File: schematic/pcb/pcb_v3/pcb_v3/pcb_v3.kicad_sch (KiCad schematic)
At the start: 52 parts, among them IC1 FT232RNQ-TRAY, J1 5V, J2 SERVO, J3 MAVLINK, J4 DISPLAY, J5 SER. SERVO, J6 MAG., J7 U.FL-R, J8 Conn_01x05_Pin, J9 Conn_01x05_Pin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

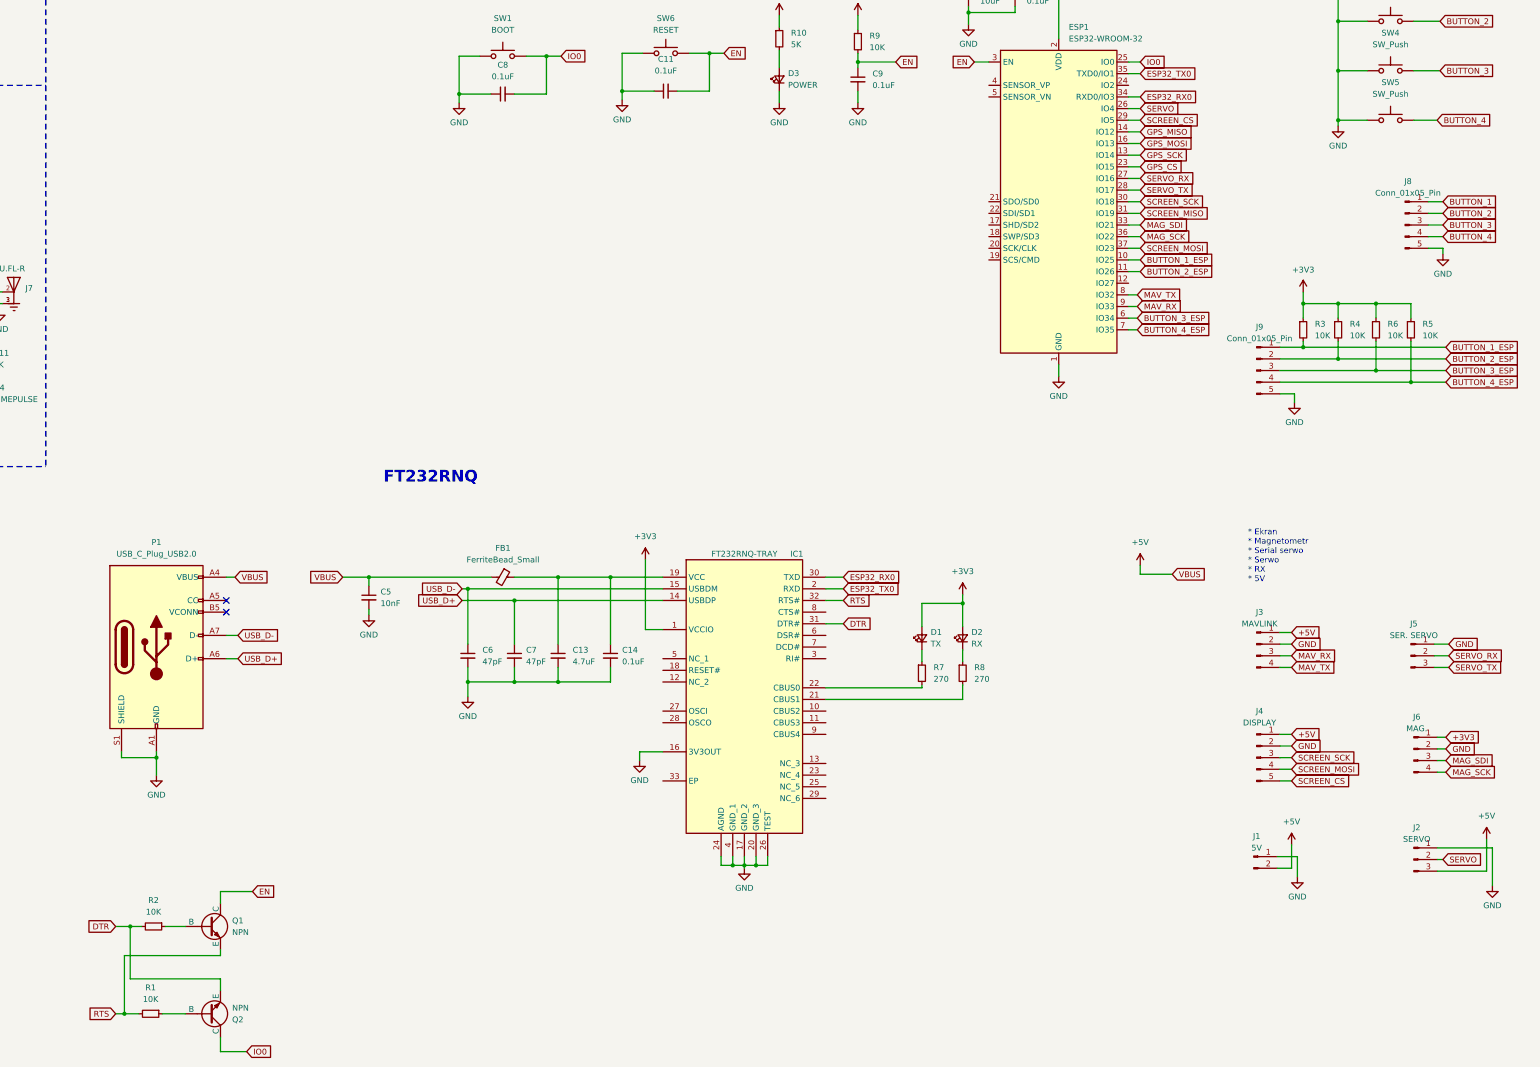
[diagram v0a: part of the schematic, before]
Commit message: pcb update, bluetooth bridge working
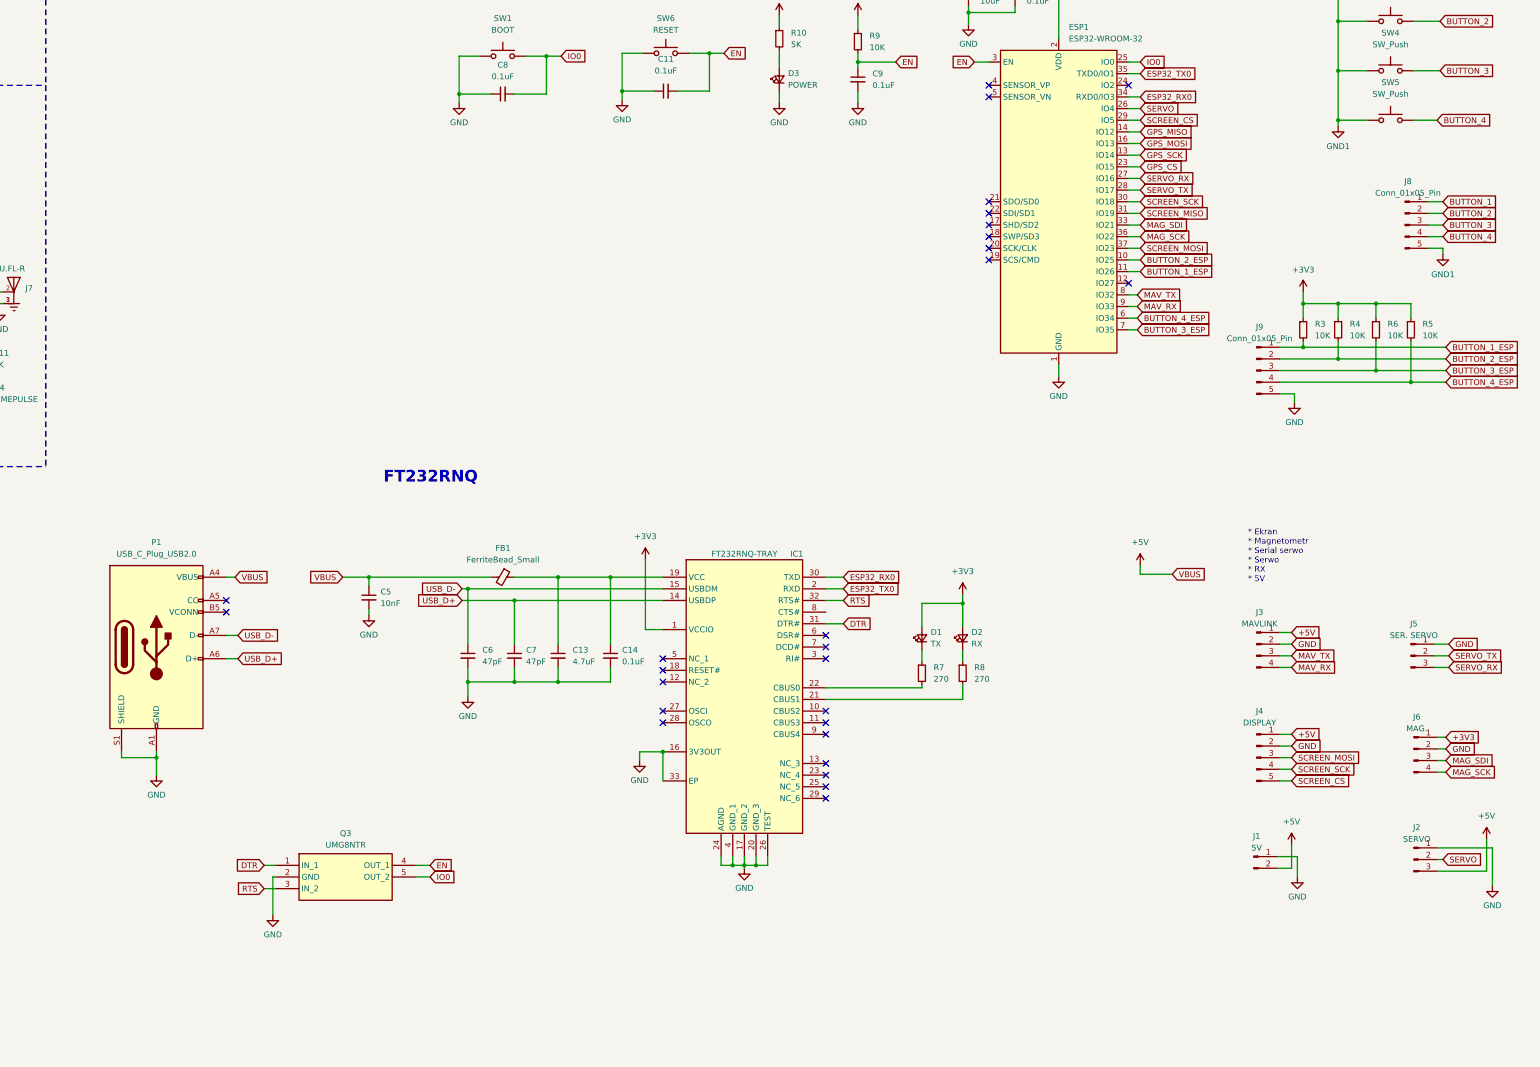
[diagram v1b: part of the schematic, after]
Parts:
- removed Q1, Q2: NPN, Package_TO_SOT_SMD:TSOT-23, symbol Simulation_SPICE:NPN
- removed R1, R2: 10K, Resistor_SMD:R_0805_2012Metric, symbol Device:R_Small
- added Q3: UMG8NTR, Package_TO_SOT_SMD:SOT-353_SC-70-5, symbol Transistor_BJT:UMG8NTR
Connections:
- net BUTTON_1_ESP: now also ESP1.11 (IO26); no longer ESP1.10 (IO25)
- net BUTTON_2_ESP: now also ESP1.10 (IO25); no longer ESP1.11 (IO26)
- net BUTTON_3_ESP: now also ESP1.7 (IO35); no longer ESP1.6 (IO34)
- net BUTTON_4_ESP: now also ESP1.6 (IO34); no longer ESP1.7 (IO35)
- net DTR: now also Q3.1 (IN_1)
- net EN: now also Q3.4 (OUT_1)
- net GND: now also IC1.33 (EP), Q3.2 (GND); no longer J8.5 (Pin_5), SW2.1, SW3.1, SW4.1, SW5.1
- net IO0: now also Q3.5 (OUT_2)
- net MAV_RX: now also J3.4 (Pin_4); no longer J3.3 (Pin_3)
- net MAV_TX: now also J3.3 (Pin_3); no longer J3.4 (Pin_4)
- net RTS: now also Q3.3 (IN_2)
- net SCREEN_MOSI: now also J4.3 (Pin_3); no longer J4.4 (Pin_4)
- net SCREEN_SCK: now also J4.4 (Pin_4); no longer J4.3 (Pin_3)
- net SERVO_RX: now also J5.3 (Pin_3); no longer J5.2 (Pin_2)
- net SERVO_TX: now also J5.2 (Pin_2); no longer J5.3 (Pin_3)
- new net GND1: J8.5 (Pin_5), SW2.1, SW3.1, SW4.1, SW5.1
- no-connect marks 9 -> 34

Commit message: pcb updates
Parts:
- removed Q3: UMG8NTR, Package_TO_SOT_SMD:SOT-353_SC-70-5, symbol Transistor_BJT:UMG8NTR
- added BT1: Battery_Cell, Battery:BatteryHolder_Keystone_1060_1x2032, symbol Device:Battery_Cell
- added C15: 0.1uF, Capacitor_SMD:C_0805_2012Metric, symbol Device:C_Small
- added J10: Micro_SD_Card, symbol Connector:Micro_SD_Card
- added Q1, Q2: NPN, Package_TO_SOT_SMD:TSOT-23, symbol Simulation_SPICE:NPN
- added R1, R2: 10K, Resistor_SMD:R_0805_2012Metric, symbol Device:R_Small
- C11, C8: value 0.1uF -> 47pF
- C2, C4: value 10uF -> 1uF
- J7: footprint HRS_U.FL-R-SMT-1(10) -> U.FL-R-SMT-1_10:HRS_U.FL-R-SMT-1(10)
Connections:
- net +3V3: no longer U1.22 (V_BCKP)
- net DTR: now also Q2.3 (E), R2.2
- net EN: now also Q1.1 (C)
- net GND: now also BT1.2 (-), C15.1; no longer IC1.16 (3V3OUT)
- net IO0: now also Q2.1 (C)
- net RTS: now also Q1.3 (E), R1.2
- new net: C15.2, IC1.16 (3V3OUT)
- new net: BT1.1 (+), U1.22 (V_BCKP)
- new net: Q2.2 (B), R1.1
- new net: Q1.2 (B), R2.1
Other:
- note added: "3,3V LDO"
- note added: "FT232RNQ USB <-> UART"
- note added: "UBLOX M9N GPS"
- note removed: "3.3 LDO"
- note removed: "FT232RNQ"
- note removed: "UBLOX M9N"
- title: (none) -> Tracker PCB
- moved on the sheet: C1, C10, C11, C12, C13, C14, C2, C3, C4, C5, C6, C7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
